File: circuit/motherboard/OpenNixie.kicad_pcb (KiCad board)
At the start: 2 copper layers, 152 x 55 mm, 63 parts, among them J1 Jack-DC, J2 Nixie_Conn_12P, J3 Nixie_Conn_12P, J4 Nixie_Conn_12P, J5 Nixie_Conn_12P, J6 Conn_01x05, Q1 MPSA42, Q10 MPSA42, Q11 MPSA42, Q12 MPSA42, Q13 MPSA42, Q14 MPSA42, Q15 MPSA42, Q16 MPSA42, Q2 TK8P65W, Q3 MPSA42, Q4 MPSA42, Q5 MPSA42, Q6 MPSA42, Q7 MPSA42, Q8 MPSA42, Q9 MPSA42, U1 AMS1117, U2 MAX1771CSA, U3 74HC595, U4 74HC595

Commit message: Some integration works
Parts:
- removed the G*** at (147.5, 77.0)
- removed J6: Conn_01x05, Connector_PinHeader_2.54mm:PinHeader_1x05_P2.54mm_Vertical
- added BT1: 3V, Battery:BatteryHolder_LINX_BAT-HLD-012-SMT, B.Cu at (138.8, 96.7)
- added C4: 10uF, Capacitor_THT:CP_Radial_D5.0mm_P2.50mm, F.Cu at (134.4, 80.4)
- added C6: 20pF, Capacitor_THT:C_Disc_D3.0mm_W2.0mm_P2.50mm, B.Cu at (176.7, 82.6)
- added C7: 0.1uF, Capacitor_THT:C_Disc_D3.0mm_W2.0mm_P2.50mm, B.Cu at (142.1, 78.2)
- added C8: 20pF, Capacitor_THT:C_Disc_D3.0mm_W2.0mm_P2.50mm, B.Cu at (171.3, 82.6)
- added R2: 10k, Resistor_THT:R_Axial_DIN0204_L3.6mm_D1.6mm_P7.62mm_Horizontal, B.Cu at (166.2, 78.2)
- added R4: 10k, Resistor_THT:R_Axial_DIN0204_L3.6mm_D1.6mm_P7.62mm_Horizontal, B.Cu at (166.2, 75.6)
- added R9: 10k, Resistor_THT:R_Axial_DIN0204_L3.6mm_D1.6mm_P7.62mm_Horizontal, F.Cu at (132.4, 87.6)
- added SW1: SW_Push, Button_Switch_SMD:SW_SPST_FSMSM, F.Cu at (128.8, 73.4)
- added U2: JDY-34, Connector_PinSocket_2.54mm:PinSocket_1x05_P2.54mm_Vertical, F.Cu at (193.8, 74.9)
- added U4: AT89C52, Package_DIP:DIP-40_W15.24mm, F.Cu at (140.8, 87.6)
- added U5: DS3231M, Package_SO:SOIC-16W_7.5x10.3mm_P1.27mm, B.Cu at (150.6, 80.0)
- added Y1: 11.0592MHz, Crystal:Crystal_HC18-U_Vertical, B.Cu at (161.1, 82.6)
- R1: footprint Resistor_THT:R_Axial_DIN0204_L3.6mm_D1.6mm_P5.08mm_Horizontal -> Resistor_THT:R_Axial_DIN0204_L3.6mm_D1.6mm_P7.62mm_Horizontal
- R10: renamed from R7; footprint Resistor_THT:R_Axial_DIN0204_L3.6mm_D1.6mm_P5.08mm_Horizontal -> Resistor_THT:R_Axial_DIN0204_L3.6mm_D1.6mm_P7.62mm_Horizontal
- R11: renamed from R8; footprint Resistor_THT:R_Axial_DIN0204_L3.6mm_D1.6mm_P5.08mm_Horizontal -> Resistor_THT:R_Axial_DIN0204_L3.6mm_D1.6mm_P7.62mm_Horizontal
- R12: renamed from R9; footprint Resistor_THT:R_Axial_DIN0204_L3.6mm_D1.6mm_P5.08mm_Horizontal -> Resistor_THT:R_Axial_DIN0204_L3.6mm_D1.6mm_P7.62mm_Horizontal
- R13: renamed from R10; footprint Resistor_THT:R_Axial_DIN0204_L3.6mm_D1.6mm_P5.08mm_Horizontal -> Resistor_THT:R_Axial_DIN0204_L3.6mm_D1.6mm_P7.62mm_Horizontal
- R14: renamed from R11; footprint Resistor_THT:R_Axial_DIN0204_L3.6mm_D1.6mm_P5.08mm_Horizontal -> Resistor_THT:R_Axial_DIN0204_L3.6mm_D1.6mm_P7.62mm_Horizontal
- R15: renamed from R12; footprint Resistor_THT:R_Axial_DIN0204_L3.6mm_D1.6mm_P5.08mm_Horizontal -> Resistor_THT:R_Axial_DIN0204_L3.6mm_D1.6mm_P7.62mm_Horizontal
- R16: renamed from R13; footprint Resistor_THT:R_Axial_DIN0204_L3.6mm_D1.6mm_P5.08mm_Horizontal -> Resistor_THT:R_Axial_DIN0204_L3.6mm_D1.6mm_P7.62mm_Horizontal
- R17: renamed from R14; footprint Resistor_THT:R_Axial_DIN0204_L3.6mm_D1.6mm_P5.08mm_Horizontal -> Resistor_THT:R_Axial_DIN0204_L3.6mm_D1.6mm_P7.62mm_Horizontal
- R18: renamed from R15; footprint Resistor_THT:R_Axial_DIN0204_L3.6mm_D1.6mm_P5.08mm_Horizontal -> Resistor_THT:R_Axial_DIN0204_L3.6mm_D1.6mm_P7.62mm_Horizontal
- R19: renamed from R16; footprint Resistor_THT:R_Axial_DIN0204_L3.6mm_D1.6mm_P5.08mm_Horizontal -> Resistor_THT:R_Axial_DIN0204_L3.6mm_D1.6mm_P7.62mm_Horizontal
- R20: renamed from R17; value 47k -> 20k; footprint Resistor_THT:R_Axial_DIN0204_L3.6mm_D1.6mm_P5.08mm_Horizontal -> Resistor_THT:R_Axial_DIN0207_L6.3mm_D2.5mm_P10.16mm_Horizontal
- R21: renamed from R18; value 47k -> 20k; footprint Resistor_THT:R_Axial_DIN0204_L3.6mm_D1.6mm_P5.08mm_Horizontal -> Resistor_THT:R_Axial_DIN0207_L6.3mm_D2.5mm_P10.16mm_Horizontal
- R22: renamed from R19; value 47k -> 20k; footprint Resistor_THT:R_Axial_DIN0204_L3.6mm_D1.6mm_P5.08mm_Horizontal -> Resistor_THT:R_Axial_DIN0207_L6.3mm_D2.5mm_P10.16mm_Horizontal
- R23: renamed from R20; value 47k -> 20k; footprint Resistor_THT:R_Axial_DIN0204_L3.6mm_D1.6mm_P5.08mm_Horizontal -> Resistor_THT:R_Axial_DIN0207_L6.3mm_D2.5mm_P10.16mm_Horizontal
- R24: renamed from R21; footprint Resistor_THT:R_Axial_DIN0204_L3.6mm_D1.6mm_P5.08mm_Horizontal -> Resistor_THT:R_Axial_DIN0204_L3.6mm_D1.6mm_P7.62mm_Horizontal
- R25: renamed from R22; footprint Resistor_THT:R_Axial_DIN0204_L3.6mm_D1.6mm_P5.08mm_Horizontal -> Resistor_THT:R_Axial_DIN0204_L3.6mm_D1.6mm_P7.62mm_Horizontal
- R26: renamed from R23; footprint Resistor_THT:R_Axial_DIN0204_L3.6mm_D1.6mm_P5.08mm_Horizontal -> Resistor_THT:R_Axial_DIN0204_L3.6mm_D1.6mm_P7.62mm_Horizontal
- R27: renamed from R24; footprint Resistor_THT:R_Axial_DIN0204_L3.6mm_D1.6mm_P5.08mm_Horizontal -> Resistor_THT:R_Axial_DIN0204_L3.6mm_D1.6mm_P7.62mm_Horizontal
- R3: renamed from R2; footprint Resistor_THT:R_Axial_DIN0204_L3.6mm_D1.6mm_P5.08mm_Horizontal -> Resistor_THT:R_Axial_DIN0204_L3.6mm_D1.6mm_P7.62mm_Horizontal
- R5: renamed from R3; footprint Resistor_THT:R_Axial_DIN0204_L3.6mm_D1.6mm_P5.08mm_Horizontal -> Resistor_THT:R_Axial_DIN0204_L3.6mm_D1.6mm_P7.62mm_Horizontal
- R6: renamed from R4; footprint Resistor_THT:R_Axial_DIN0204_L3.6mm_D1.6mm_P5.08mm_Horizontal -> Resistor_THT:R_Axial_DIN0204_L3.6mm_D1.6mm_P7.62mm_Horizontal
- R7: renamed from R5; footprint Resistor_THT:R_Axial_DIN0204_L3.6mm_D1.6mm_P5.08mm_Horizontal -> Resistor_THT:R_Axial_DIN0204_L3.6mm_D1.6mm_P7.62mm_Horizontal
- moved U6 91.1 mm to (184.0, 115.6)
- moved U7 88.2 mm to (206.1, 115.6)
- moved R11 82.4 mm to (134.5, 115.4), turned to 90 degrees
- moved Q4 80.1 mm to (138.1, 112.0)
- moved R12 75.7 mm to (144.3, 115.4), turned to 90 degrees
- moved Q12 74.9 mm to (92.3, 108.2)
- moved Q8 74.0 mm to (119.3, 108.3)
- moved Q5 73.8 mm to (147.9, 112.0)
- moved Q10 69.8 mm to (105.9, 108.1)
- moved R19 68.6 mm to (97.5, 112.2), turned to 180 degrees
- moved R15 67.6 mm to (124.3, 112.2), turned to 180 degrees
- moved Q9 65.4 mm to (119.3, 116.9)
- moved R17 63.6 mm to (110.9, 112.2), turned to 180 degrees
- moved R16 58.9 mm to (124.4, 120.8), turned to 180 degrees
- moved Q3 58.3 mm to (92.3, 116.7)
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- renumbered C4 to C5, R6 to R8, U2 to U3, U3 to U6, U4 to U7
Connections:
- net /+5v renamed /+5V
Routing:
- net /SEG_P7: track 291.1 -> 147.5 mm, vias 1 -> 0
- net /ENABLE: track 63.0 -> 198.0 mm
- net /+5V: track 108.4 -> 242.3 mm, vias 1 -> 2
- net /SEG_P9: track 276.0 -> 153.2 mm
- net /SR_BIT_P1: track 24.8 -> 137.1 mm, vias 0 -> 4
- net /SR_BIT_P0: track 33.1 -> 138.2 mm, vias 0 -> 1
- net /SR_SEG_P8: track 45.8 -> 142.8 mm
- net /SEG_P8: track 268.7 -> 178.7 mm, vias 2 -> 1
- net /SR_SEG_P2: track 153.9 -> 66.3 mm
- net /SR_SEG_P1: track 136.1 -> 50.4 mm
- net /SR_SEG_P4: track 102.5 -> 28.7 mm
- net /SR_SEG_P3: track 114.2 -> 45.2 mm
- net /SEG_P3: track 226.2 -> 159.3 mm, vias 0 -> 3
- net /SR_SEG_P9: track 50.1 -> 111.2 mm
- net /SR_BIT_P3: track 97.6 -> 38.3 mm, vias 1 -> 0
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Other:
- board text added: "locked"
- board text removed: "HIGH VOLTAGE DANGER DO NOT TOUCH DURING OPERATION"
- board text removed: "LCH DAT CLK +5V GND"
- board text removed: "OpenNixie@ibcl.us github.com/bclswl0827/OpenNixie"

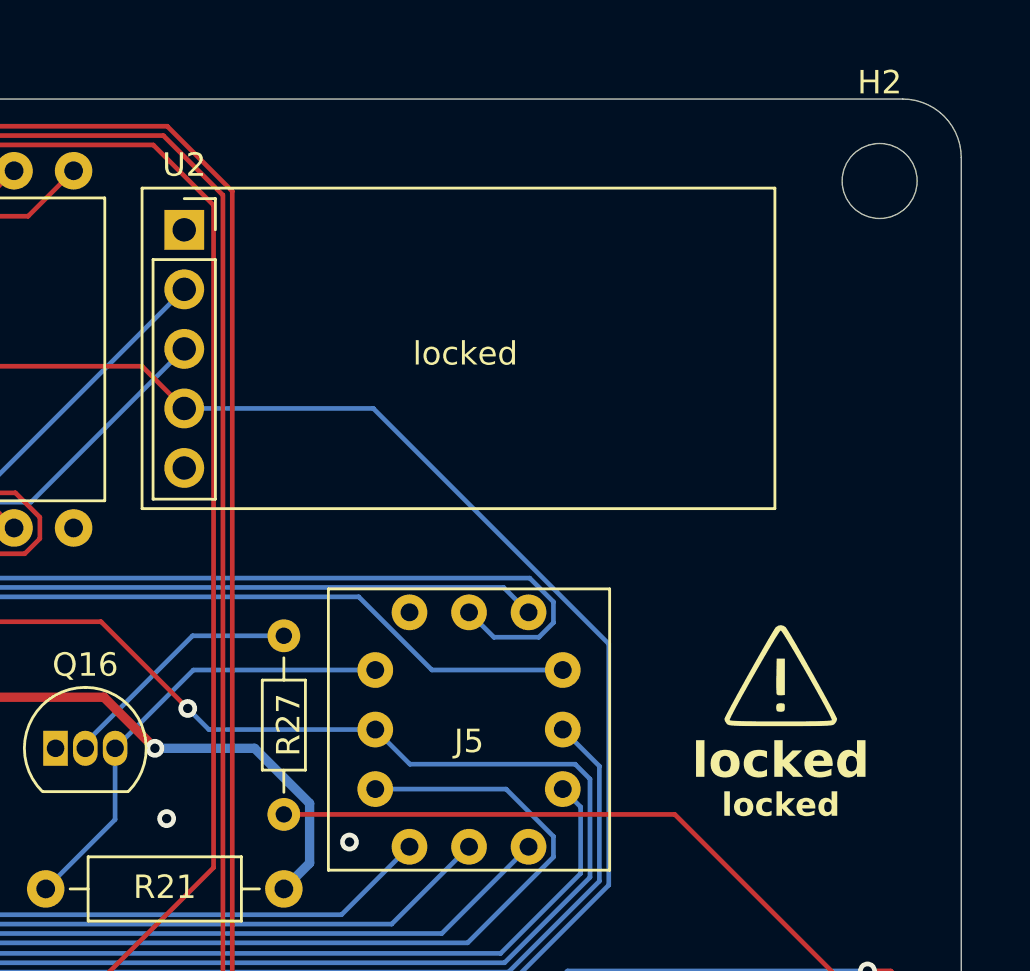
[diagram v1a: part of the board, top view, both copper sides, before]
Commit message: Move bluetooth to bottom
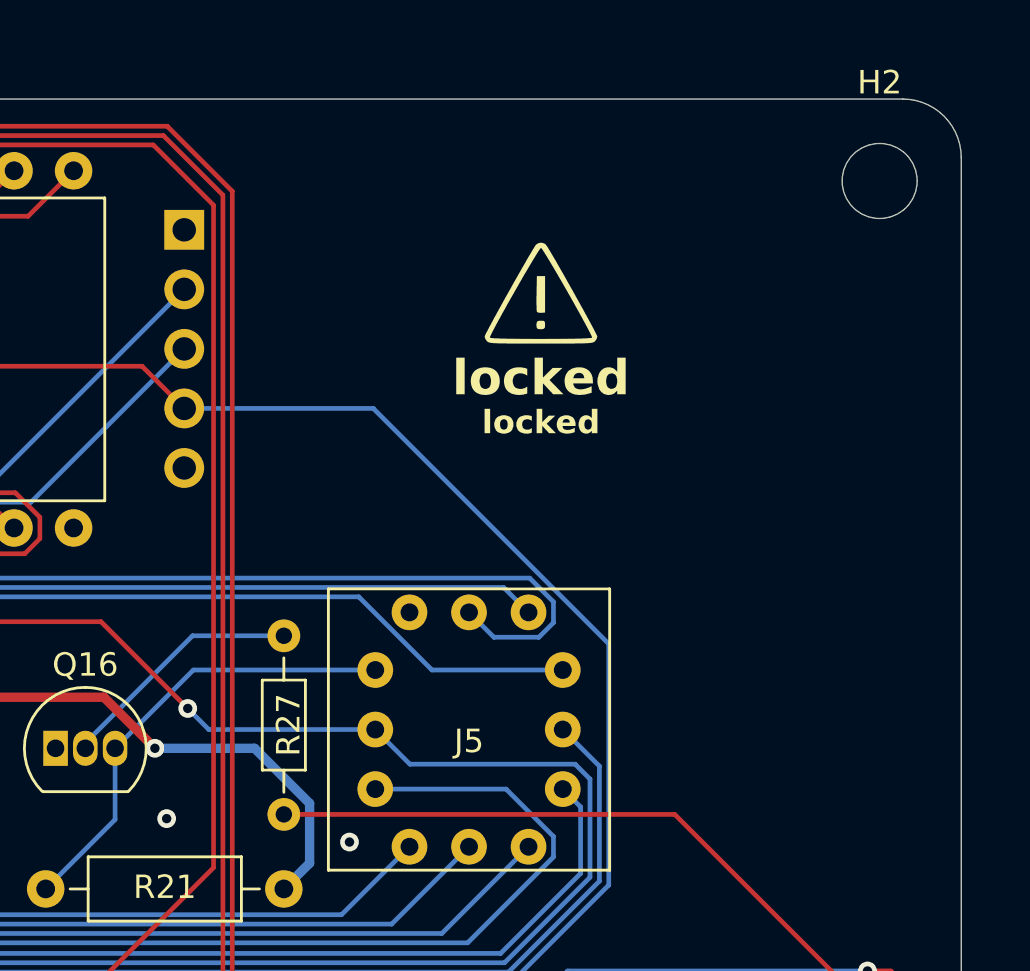
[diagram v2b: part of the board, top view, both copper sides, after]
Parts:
- U2: moved to B.Cu
- moved G*** 19.3 mm to (209.0, 77.6)
- turned U2 to 180 degrees
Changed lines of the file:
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@@
   )
   (footprint "Nixie_Clock:Icon_Risk" locked (layer "F.Cu")
-    (at 219.2 93.95)
+    (at 208.97 77.63)
     (attr board_only exclude_from_pos_files exclude_from_bom)
     (fp_text reference "G***" (at 0 0) (layer "F.SilkS") hide
@@
     )
   )
-  (footprint "Connector_PinSocket_2.54mm:PinSocket_1x05_P2.54mm_Vertical" locked (layer "F.Cu")
-    (at 193.75 74.88)
-    (descr "Through hole straight socket strip, 1x05, 2.54mm pitch, single row (from Kicad 4.0.7), script generated")
-    (tags "Through hole socket strip THT 1x05 2.54mm single row")
-    (property "Sheetfile" "OpenNixie.kicad_sch")
-    (property "Sheetname" "")
-    (attr through_hole)
-    (fp_text reference "U2" (at 0 -2.77) (layer "F.SilkS")
-        (effects (font (size 1 1) (thickness 0.15)))
-    )
-    (fp_text value "JDY-34" (at 0 12.93) (layer "F.Fab")
-        (effects (font (size 1 1) (thickness 0.15)))
-    )
-    (fp_text user "${REFERENCE}" (at 0 5.08 90) (layer "F.Fab")
-        (effects (font (size 1 1) (thickness 0.15)))
-    )
-    (fp_line (start -1.33 1.27) (end -1.33 11.49)
-      (stroke (width 0.12) (type solid)) (layer "F.SilkS"))
-    (fp_line (start -1.33 1.27) (end 1.33 1.27)
-      (stroke (width 0.12) (type solid)) (layer "F.SilkS"))
-    (fp_line (start -1.33 11.49) (end 1.33 11.49)
-      (stroke (width 0.12) (type solid)) (layer "F.SilkS"))
-    (fp_line (start 0 -1.33) (end 1.33 -1.33)
-      (stroke (width 0.12) (type solid)) (layer "F.SilkS"))
-    (fp_line (start 1.33 -1.33) (end 1.33 0)
-      (stroke (width 0.12) (type solid)) (layer "F.SilkS"))
-    (fp_line (start 1.33 1.27) (end 1.33 11.49)
-      (stroke (width 0.12) (type solid)) (layer "F.SilkS"))
-    (fp_line (start -1.8 -1.8) (end 1.75 -1.8)
-      (stroke (width 0.05) (type solid)) (layer "F.CrtYd"))
-    (fp_line (start -1.8 11.9) (end -1.8 -1.8)
-      (stroke (width 0.05) (type solid)) (layer "F.CrtYd"))
-    (fp_line (start 1.75 -1.8) (end 1.75 11.9)
-      (stroke (width 0.05) (type solid)) (layer "F.CrtYd"))
-    (fp_line (start 1.75 11.9) (end -1.8 11.9)
-      (stroke (width 0.05) (type solid)) (layer "F.CrtYd"))
-    (fp_line (start -1.27 -1.27) (end 0.635 -1.27)
-      (stroke (width 0.1) (type solid)) (layer "F.Fab"))
-    (fp_line (start -1.27 11.43) (end -1.27 -1.27)
-      (stroke (width 0.1) (type solid)) (layer "F.Fab"))
-    (fp_line (start 0.635 -1.27) (end 1.27 -0.635)
-      (stroke (width 0.1) (type solid)) (layer "F.Fab"))
-    (fp_line (start 1.27 -0.635) (end 1.27 11.43)
-      (stroke (width 0.1) (type solid)) (layer "F.Fab"))
-    (fp_line (start 1.27 11.43) (end -1.27 11.43)
-      (stroke (width 0.1) (type solid)) (layer "F.Fab"))
-    (pad "1" thru_hole rect locked (at 0 0) (size 1.7 1.7) (drill 1) (layers "*.Cu" "*.Mask")
-      (net 71 "unconnected-(U2-STATE-Pad1)") (pinfunction "STATE") (pintype "output+no_connect"))
-    (pad "2" thru_hole oval locked (at 0 2.54) (size 1.7 1.7) (drill 1) (layers "*.Cu" "*.Mask")
-      (net 72 "/BLE_TXD") (pinfunction "TXD") (pintype "bidirectional"))
-    (pad "3" thru_hole oval locked (at 0 5.08) (size 1.7 1.7) (drill 1) (layers "*.Cu" "*.Mask")
-      (net 73 "/BLE_RXD") (pinfunction "RXD") (pintype "bidirectional"))
-    (pad "4" thru_hole oval locked (at 0 7.62) (size 1.7 1.7) (drill 1) (layers "*.Cu" "*.Mask")
-      (net 3 "/+5V") (pinfunction "VCC") (pintype "power_in"))
-    (pad "5" thru_hole oval locked (at 0 10.16) (size 1.7 1.7) (drill 1) (layers "*.Cu" "*.Mask")
-      (net 1 "GND") (pinfunction "GND") (pintype "power_in"))
-    (model "${KICAD6_3DMODEL_DIR}/Connector_PinSocket_2.54mm.3dshapes/PinSocket_1x05_P2.54mm_Vertical.wrl"
-      (offset (xyz 0 0 0))
-      (scale (xyz 1 1 1))
-      (rotate (xyz 0 0 0))
-    )
-  )
   (footprint "Resistor_THT:R_Axial_DIN0204_L3.6mm_D1.6mm_P7.62mm_Horizontal" locked (layer "F.Cu")
     (at 124.285 112.155153 180)
@@
     )
   )
+  (footprint "Connector_PinSocket_2.54mm:PinSocket_1x05_P2.54mm_Vertical" locked (layer "B.Cu")
+    (at 193.75 74.88 180)
+    (descr "Through hole straight socket strip, 1x05, 2.54mm pitch, single row (from Kicad 4.0.7), script generated")
+    (tags "Through hole socket strip THT 1x05 2.54mm single row")
+    (property "Sheetfile" "OpenNixie.kicad_sch")
+    (property "Sheetname" "")
+    (attr through_hole)
+    (fp_text reference "U2" (at 0 2.77) (layer "B.SilkS")
+        (effects (font (size 1 1) (thickness 0.15)) (justify mirror))
+    )
+    (fp_text value "JDY-34" (at 0 -12.93) (layer "B.Fab")
+        (effects (font (size 1 1) (thickness 0.15)) (justify mirror))
+    )
+    (fp_text user "${REFERENCE}" (at 0 -5.08 90) (layer "B.Fab")
+        (effects (font (size 1 1) (thickness 0.15)) (justify mirror))
+    )
+    (fp_line (start -1.33 -11.49) (end 1.33 -11.49)
+      (stroke (width 0.12) (type solid)) (layer "B.SilkS"))
+    (fp_line (start -1.33 -1.27) (end -1.33 -11.49)
+      (stroke (width 0.12) (type solid)) (layer "B.SilkS"))
+    (fp_line (start -1.33 -1.27) (end 1.33 -1.27)
+      (stroke (width 0.12) (type solid)) (layer "B.SilkS"))
+    (fp_line (start 0 1.33) (end 1.33 1.33)
+      (stroke (width 0.12) (type solid)) (layer "B.SilkS"))
+    (fp_line (start 1.33 -1.27) (end 1.33 -11.49)
+      (stroke (width 0.12) (type solid)) (layer "B.SilkS"))
+    (fp_line (start 1.33 1.33) (end 1.33 0)
+      (stroke (width 0.12) (type solid)) (layer "B.SilkS"))
+    (fp_line (start -1.8 -11.9) (end -1.8 1.8)
+      (stroke (width 0.05) (type solid)) (layer "B.CrtYd"))
+    (fp_line (start -1.8 1.8) (end 1.75 1.8)
+      (stroke (width 0.05) (type solid)) (layer "B.CrtYd"))
+    (fp_line (start 1.75 -11.9) (end -1.8 -11.9)
+      (stroke (width 0.05) (type solid)) (layer "B.CrtYd"))
+    (fp_line (start 1.75 1.8) (end 1.75 -11.9)
+      (stroke (width 0.05) (type solid)) (layer "B.CrtYd"))
+    (fp_line (start -1.27 -11.43) (end -1.27 1.27)
+      (stroke (width 0.1) (type solid)) (layer "B.Fab"))
+    (fp_line (start -1.27 1.27) (end 0.635 1.27)
+      (stroke (width 0.1) (type solid)) (layer "B.Fab"))
+    (fp_line (start 0.635 1.27) (end 1.27 0.635)
+      (stroke (width 0.1) (type solid)) (layer "B.Fab"))
+    (fp_line (start 1.27 -11.43) (end -1.27 -11.43)
+      (stroke (width 0.1) (type solid)) (layer "B.Fab"))
+    (fp_line (start 1.27 0.635) (end 1.27 -11.43)
+      (stroke (width 0.1) (type solid)) (layer "B.Fab"))
+    (pad "1" thru_hole rect locked (at 0 0 180) (size 1.7 1.7) (drill 1) (layers "*.Cu" "*.Mask")
+      (net 71 "unconnected-(U2-STATE-Pad1)") (pinfunction "STATE") (pintype "output+no_connect"))
+    (pad "2" thru_hole oval locked (at 0 -2.54 180) (size 1.7 1.7) (drill 1) (layers "*.Cu" "*.Mask")
+      (net 72 "/BLE_TXD") (pinfunction "TXD") (pintype "bidirectional"))
+    (pad "3" thru_hole oval locked (at 0 -5.08 180) (size 1.7 1.7) (drill 1) (layers "*.Cu" "*.Mask")
+      (net 73 "/BLE_RXD") (pinfunction "RXD") (pintype "bidirectional"))
+    (pad "4" thru_hole oval locked (at 0 -7.62 180) (size 1.7 1.7) (drill 1) (layers "*.Cu" "*.Mask")
+      (net 3 "/+5V") (pinfunction "VCC") (pintype "power_in"))
+    (pad "5" thru_hole oval locked (at 0 -10.16 180) (size 1.7 1.7) (drill 1) (layers "*.Cu" "*.Mask")
+      (net 1 "GND") (pinfunction "GND") (pintype "power_in"))
+    (model "${KICAD6_3DMODEL_DIR}/Connector_PinSocket_2.54mm.3dshapes/PinSocket_1x05_P2.54mm_Vertical.wrl"
+      (offset (xyz 0 0 0))
+      (scale (xyz 1 1 1))
+      (rotate (xyz 0 0 0))
+    )
+  )
   (footprint "Battery:BatteryHolder_LINX_BAT-HLD-012-SMT" locked (layer "B.Cu")
     (at 138.8 96.7 120)
@@
   )
   (gr_rect locked (start 191.95 73.1) (end 218.95 86.775)
-    (stroke (width 0.12) (type default)) (fill none) (layer "F.SilkS"))
+    (stroke (width 0.12) (type default)) (fill none) (layer "B.SilkS"))
   (gr_line locked (start 77.4 69.3) (end 224.4 69.3)
     (stroke (width 0.05) (type solid)) (layer "Edge.Cuts"))
@@
   (gr_arc locked (start 226.9 121.8) (mid 226.167767 123.567767) (end 224.4 124.3)
     (stroke (width 0.05) (type default)) (layer "Edge.Cuts"))
-  (gr_text locked "CAUTION" (at 219.2 98.4) (layer "F.SilkS")
+  (gr_text locked "BLUETOOTH" (at 203.5 80.75) (layer "B.SilkS")
+    (effects (font (size 1 1) (thickness 0.15)) (justify left bottom))
+  )
+  (gr_text locked "CAUTION" (at 208.97 82.08) (layer "F.SilkS")
     (effects (font (size 1.5 1.5) (thickness 0.3) bold) (justify bottom))
   )
-  (gr_text locked "HIGH VOLTAGE" (at 219.2 100) (layer "F.SilkS")
+  (gr_text locked "HIGH VOLTAGE" (at 208.97 83.68) (layer "F.SilkS")
     (effects (font (size 1 1) (thickness 0.25) bold) (justify bottom))
   )
-  (gr_text locked "BLUETOOTH" (at 203.5 80.75) (layer "F.SilkS")
-    (effects (font (size 1 1) (thickness 0.15)) (justify left bottom))
-  )
   (via locked (at 170.6 107.4) (size 0.8) (drill 0.4) (layers "F.Cu" "B.Cu") (free) (net 1))
